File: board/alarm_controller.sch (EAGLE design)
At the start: 150 parts, among them IC3 AT24C

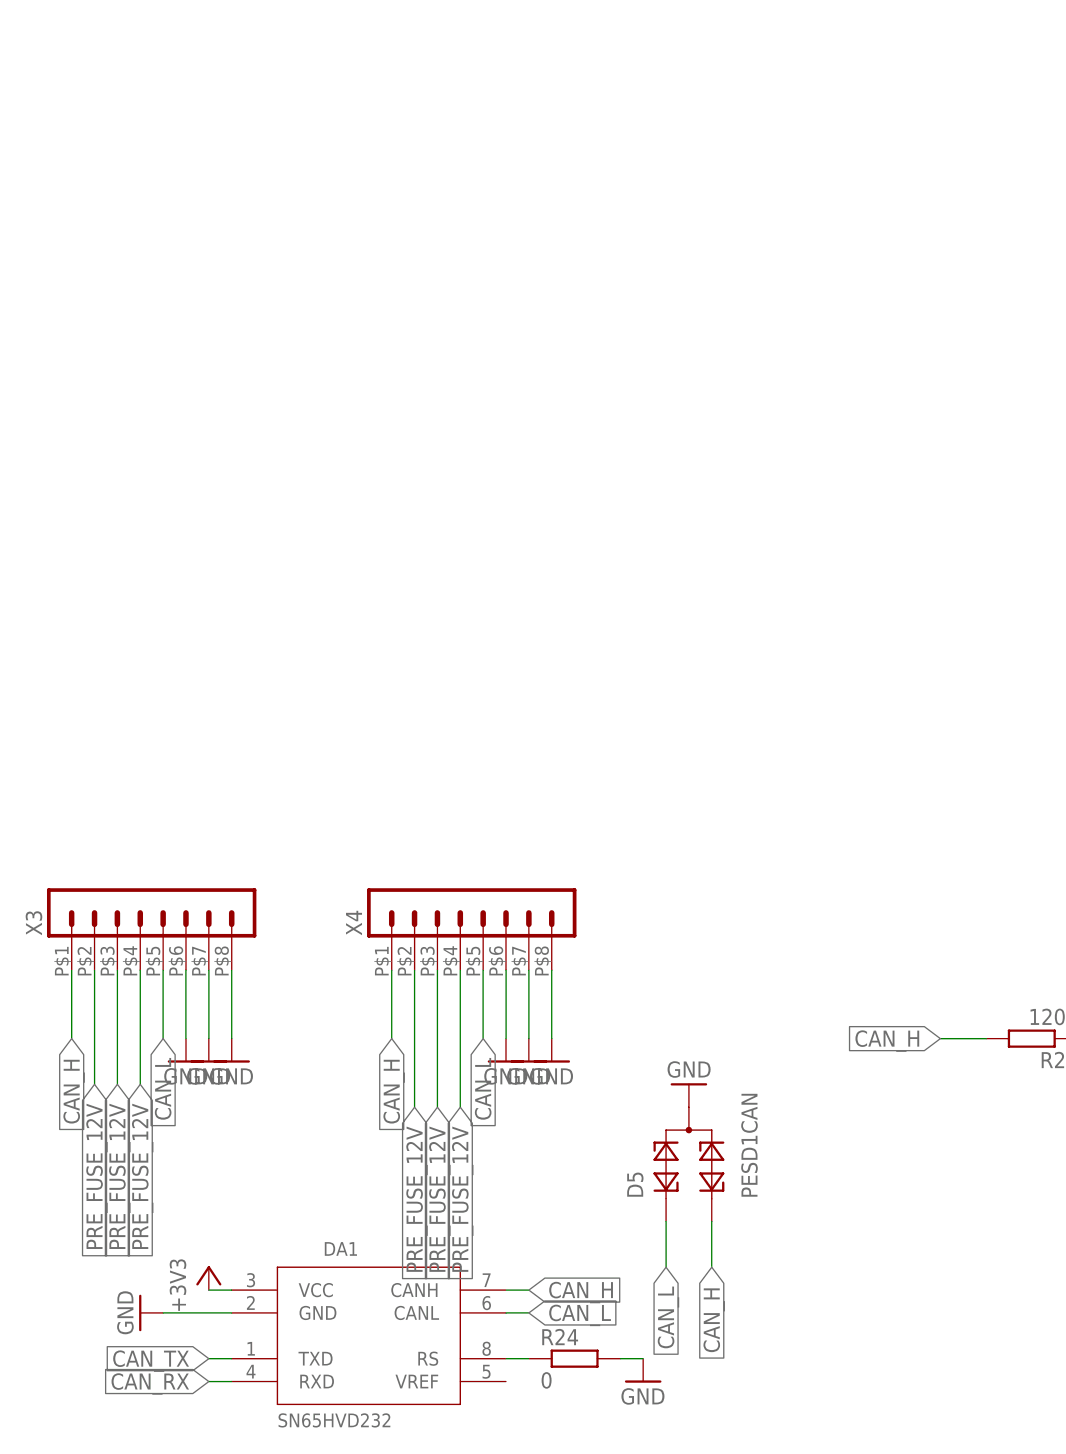
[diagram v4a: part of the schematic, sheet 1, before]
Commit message: change back to rj45 (from microfit)
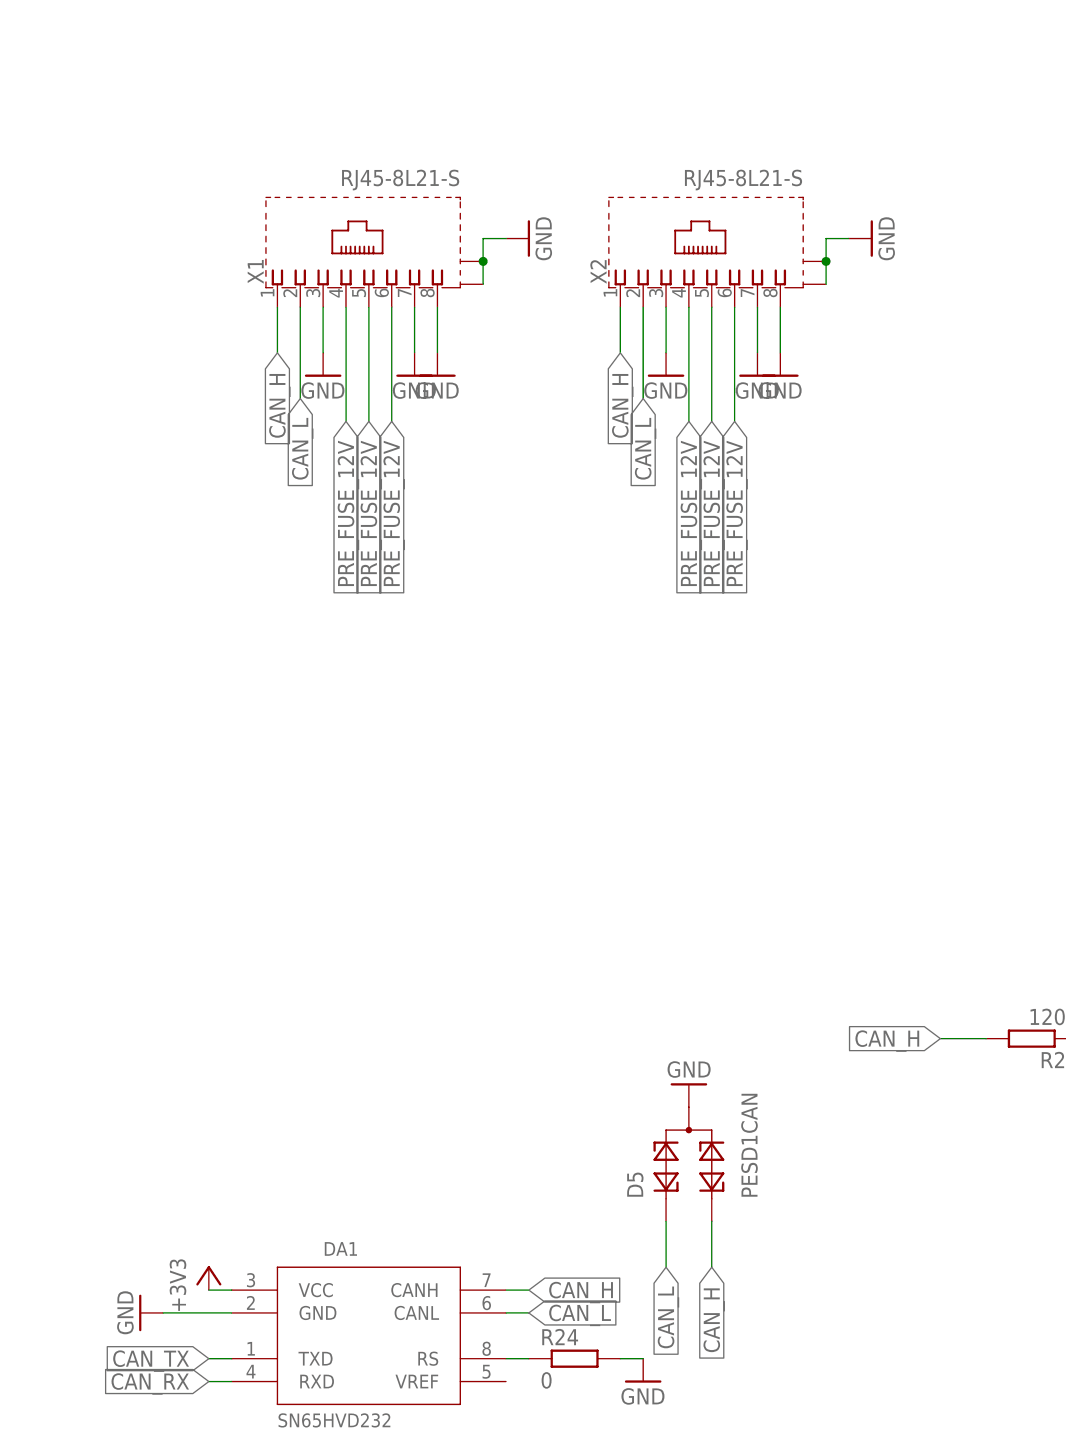
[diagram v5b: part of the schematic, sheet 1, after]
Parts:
- removed X3, X4: (no value), con-molex-micro-fit-3_0:HEADER_POS8_43045-0812
- added X1, X2: RJ45-8L21-S, con-tycoelectronics:RJ45-8L21-S
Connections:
- net CAN_H: now also X1.1, X2.1; no longer X3.1, X4.1
- net CAN_L: now also X1.2, X2.2; no longer X3.5, X4.5
- net GND: now also X1.3, X1.7, X1.8, X1.S@1, X1.S@2, X2.3, X2.7, X2.8, X2.S@1, X2.S@2; no longer X3.6, X3.7, X3.8, X4.6, X4.7, X4.8
- net PRE_FUSE_12V: now also X1.4, X1.5, X1.6, X2.4, X2.5, X2.6; no longer X3.2, X3.3, X3.4, X4.2, X4.3, X4.4

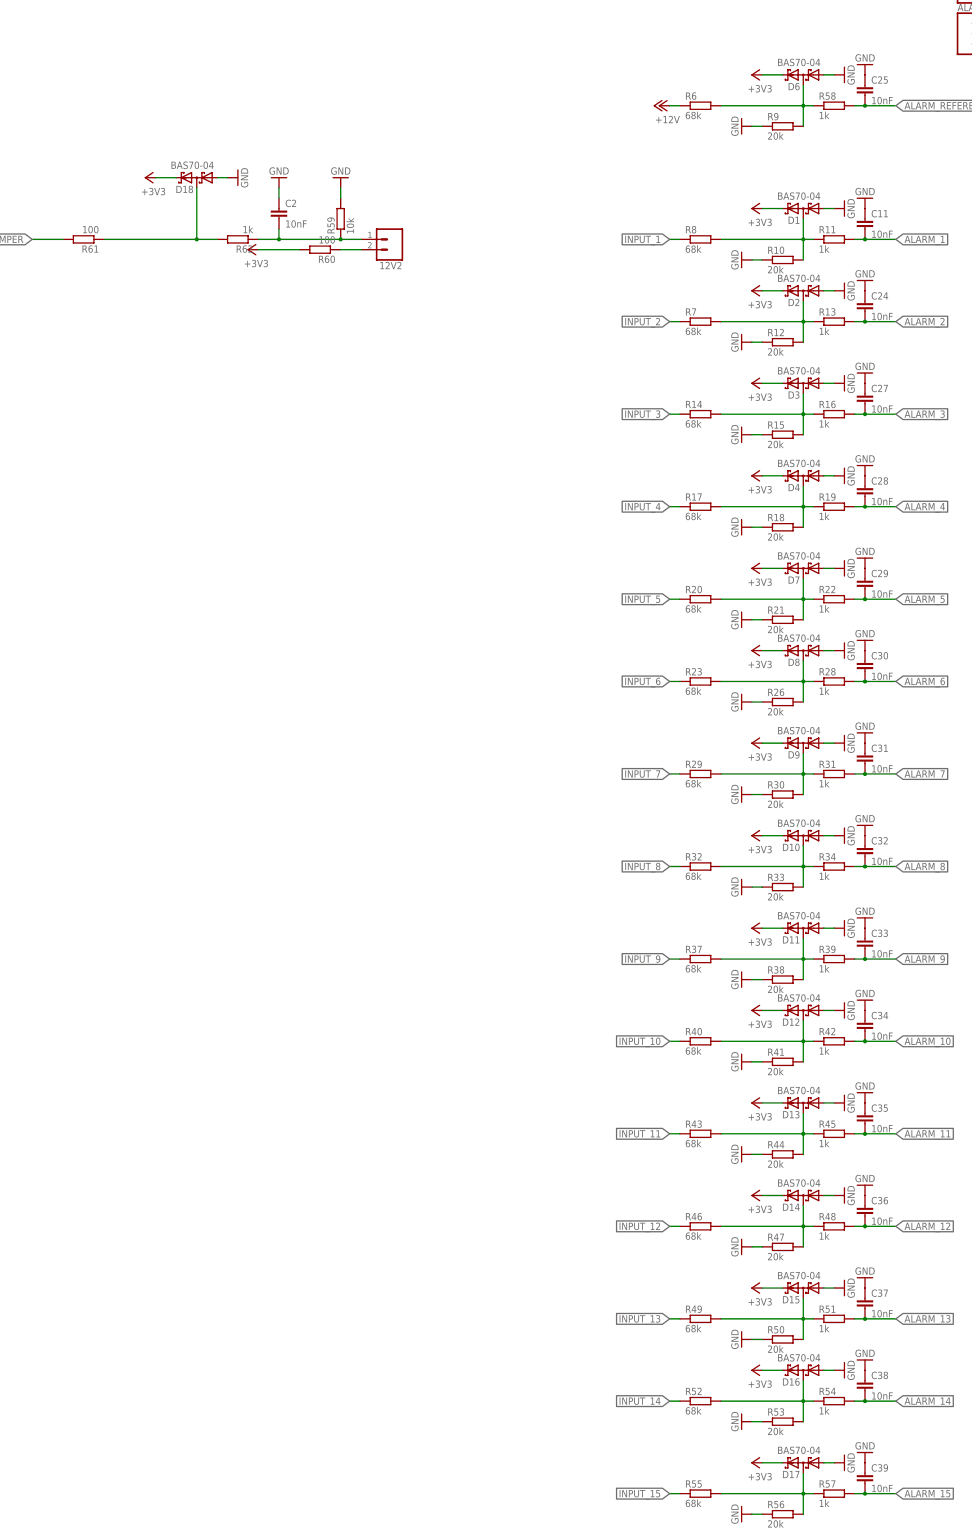
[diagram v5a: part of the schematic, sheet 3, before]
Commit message: change to packages with place drawing
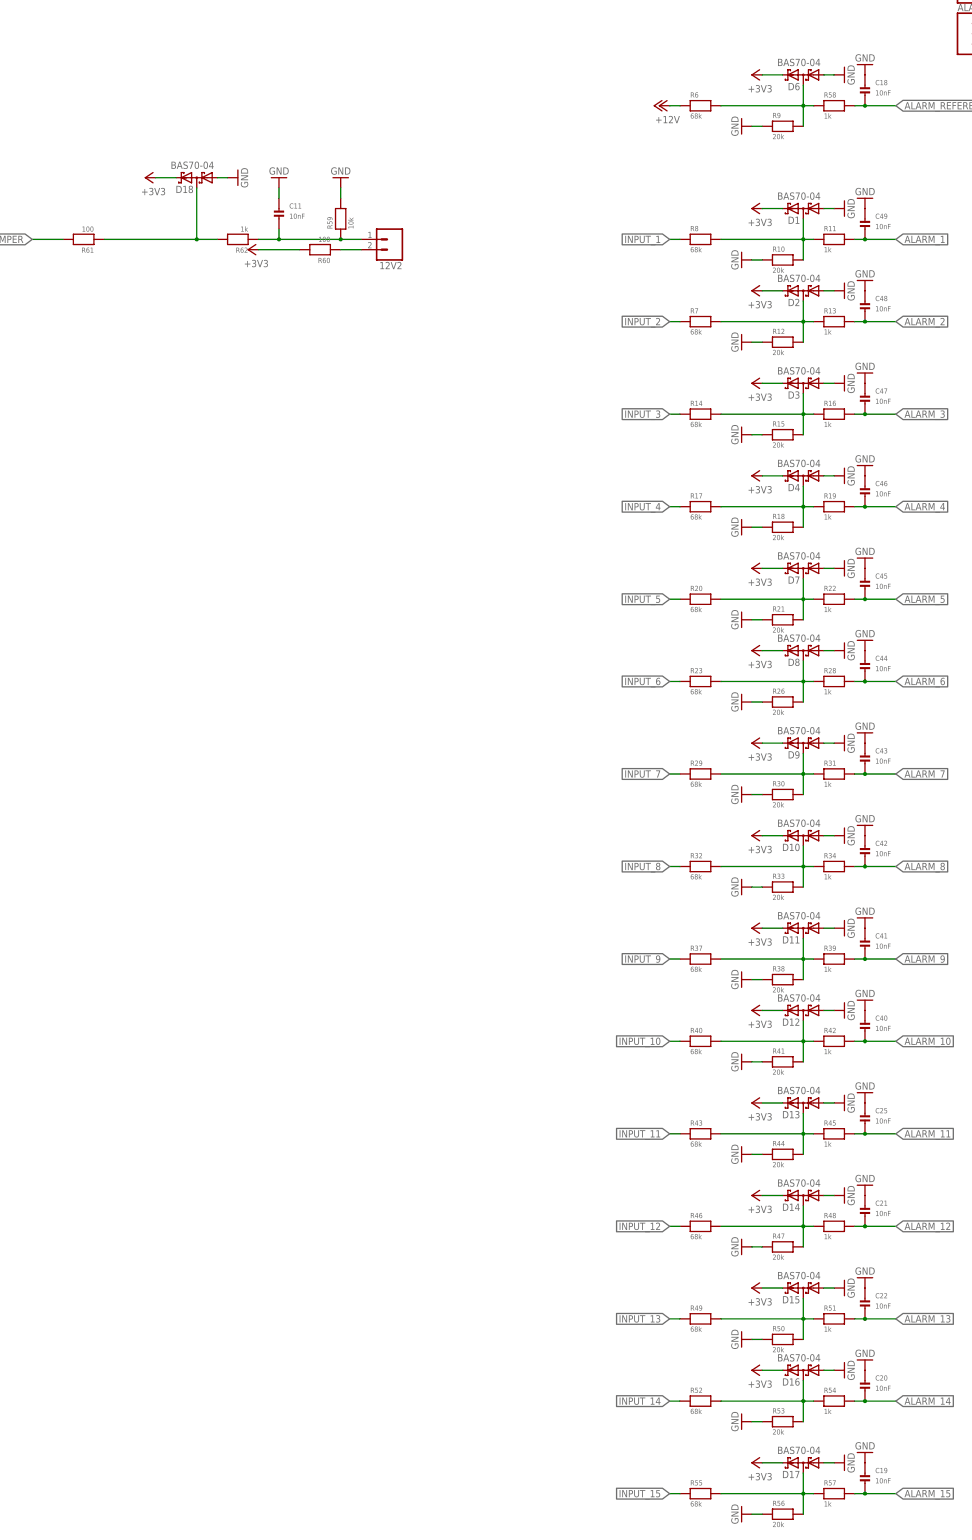
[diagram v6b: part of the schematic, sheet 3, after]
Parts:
- removed C28, C29, C30, C31, C32, C33, C34, C35, C36, C37, C38, C39: 10nF, eagle-ltspice:CC0603
- removed C3, C8: 100n, rcl:C-EUC0603
- removed C7: 1u, rcl:C-EUC0603
- added C18, C19, C20, C21, C22, C40, C41, C42, C43, C44, C45, C46, C47, C48, C49: 10nF, microbuilder:CAP_CERAMIC0603
- C1, C10, C14, C4, C5, C6, C9: device rcl:C-EUC0603 -> microbuilder:CAP_CERAMIC0603
- C11, C25: device eagle-ltspice:CC0603 -> microbuilder:CAP_CERAMIC0603
- C12, C13: value 2.2u -> 1u; device rcl:C-EUC0603 -> microbuilder:CAP_CERAMIC0603
- C15: value 1u -> 100n; device rcl:C-EUC0603 -> microbuilder:CAP_CERAMIC0603
- C16: value 1u -> 33pf; device rcl:C-EUC0603 -> microbuilder:CAP_CERAMIC0603
- C17, C23: value 33p -> 100n; device rcl:C-EUC0603 -> microbuilder:CAP_CERAMIC0603
- C2, C24: value 10nF -> 2.2u; device eagle-ltspice:CC0603 -> microbuilder:CAP_CERAMIC0603
- C26: value 100n -> 33pf; device rcl:C-EUC0603 -> microbuilder:CAP_CERAMIC0603
- C27: value 10nF -> 1u; device eagle-ltspice:CC0603 -> microbuilder:CAP_CERAMIC0603
- R1, R10, R11, R12, R13, R14, R15, R16, R17, R18, R19, R2, R20, R21, R22, R23, R24, R26, R27, R28, R29, R3, R30, R31, R32, R33, R34, R35, R37, R38, R39, R4, R40, R41, R42, R43, R44, R45, R46, R47, R48, R49, R5, R50, R51, R52, R53, R54, R55, R56, R57, R58, R59, R6, R60, R61, R62, R63, R64, R65, R66, R7, R8, R9: device rcl:R-EU_R0603 -> microbuilder:RESISTOR0603
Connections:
- net +3V3: now also C1.P$1, C10.P$1, C12.P$1, C13.P$1, C14.P$1, C15.P$1, C17.P$1, C23.P$1, C27.P$1, C4.P$1, C5.P$1, C6.P$1, C9.P$1; no longer C1.1, C10.1, C14.1, C15.1, C16.1, C26.1, C3.1, C4.1, C5.1, C6.1, C7.1, C8.1, C9.1
- net ALARM_1: now also C49.P$2; no longer C11.2
- net ALARM_10: now also C40.P$2; no longer C34.2
- net ALARM_11: now also C25.P$2; no longer C35.2
- net ALARM_12: now also C21.P$2; no longer C36.2
- net ALARM_13: now also C22.P$2; no longer C37.2
- net ALARM_14: now also C20.P$2; no longer C38.2
- net ALARM_15: now also C19.P$2; no longer C39.2
- net ALARM_2: now also C48.P$2; no longer C24.2
- net ALARM_3: now also C47.P$2; no longer C27.2
- net ALARM_4: now also C46.P$2; no longer C28.2
- net ALARM_5: now also C45.P$2; no longer C29.2
- net ALARM_6: now also C44.P$2; no longer C30.2
- net ALARM_7: now also C43.P$2; no longer C31.2
- net ALARM_8: now also C42.P$2; no longer C32.2
- net ALARM_9: now also C41.P$2; no longer C33.2
- net ALARM_REFERENCE: now also C18.P$2; no longer C25.2
- net GND: now also C1.P$2, C10.P$2, C11.P$1, C12.P$2, C13.P$2, C14.P$2, C15.P$2, C16.P$1, C17.P$2, C18.P$1, C19.P$1, C2.P$2, C20.P$1, C21.P$1, C22.P$1, C23.P$2, C24.P$2, C25.P$1, C26.P$1, C27.P$2, C4.P$2, C40.P$1, C41.P$1, C42.P$1, C43.P$1, C44.P$1, C45.P$1, C46.P$1, C47.P$1, C48.P$1, C49.P$1, C5.P$2, C6.P$2, C9.P$2; no longer C1.2, C10.2, C11.1, C12.2, C13.2, C14.2, C15.2, C16.2, C17.1, C2.1, C23.2, C24.1, C25.1, C26.2, C27.1, C28.1, C29.1, C3.2, C30.1, C31.1, C32.1, C33.1, C34.1, C35.1, C36.1, C37.1, C38.1, C39.1, C4.2, C5.2, C6.2, C7.2, C8.2, C9.2
- net N$1: now also C16.P$2; no longer C23.1
- net N$11: now also C11.P$2; no longer C2.2
- net N$2: now also C26.P$2; no longer C17.2
- net N$4: now also C2.P$1; no longer C12.1
- net N$9: now also C24.P$1; no longer C13.1
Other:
- moved on the sheet: C1, C11, C12, C13, C14, C15, C16, C25, C26, C4, C5, C6
